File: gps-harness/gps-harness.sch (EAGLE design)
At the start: 7 parts

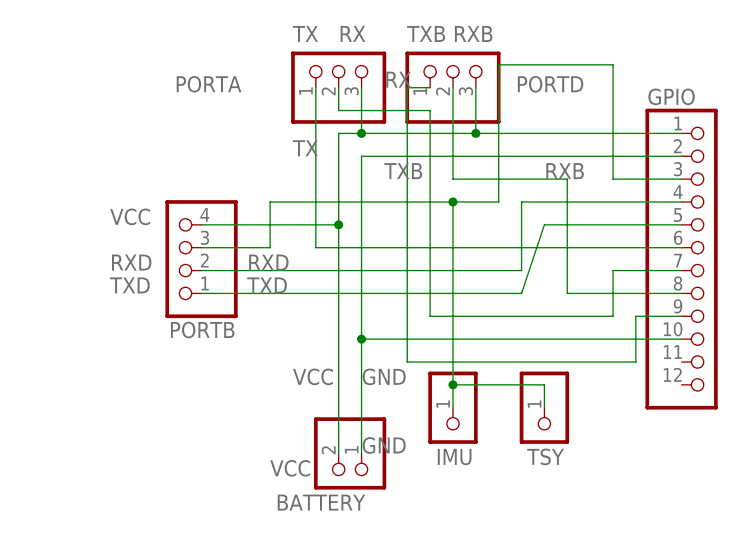
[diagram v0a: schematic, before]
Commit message: Fixed the width of the wires for battery and trying to do the mounting holes
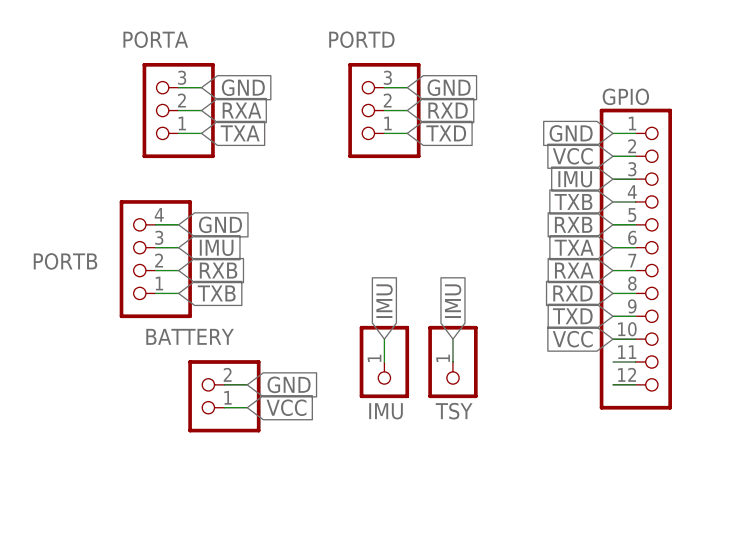
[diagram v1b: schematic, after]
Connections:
- net N$1 renamed IMU
- net RX renamed RXA
- net TX renamed TXA
- new net N$23: GPIO.11
- new net N$24: GPIO.12
- net GND: now also BATTERY.2, GPIO.1, PORTA.3, PORTB.4, PORTD.3; no longer BATTERY.1, GPIO.10, GPIO.2
- net RXB: now also GPIO.5, PORTB.2; no longer GPIO.8, PORTD.2
- net RXD: now also GPIO.8, PORTD.2; no longer GPIO.4, PORTB.2
- net TXB: now also GPIO.4, PORTB.1; no longer GPIO.9, PORTD.1
- net TXD: now also GPIO.9, PORTD.1; no longer GPIO.5, PORTB.1
- net VCC: now also BATTERY.1, GPIO.10, GPIO.2; no longer BATTERY.2, GPIO.1, PORTA.3, PORTB.4, PORTD.3
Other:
- moved on the sheet: BATTERY, GPIO, IMU, PORTA, PORTB, PORTD, TSY

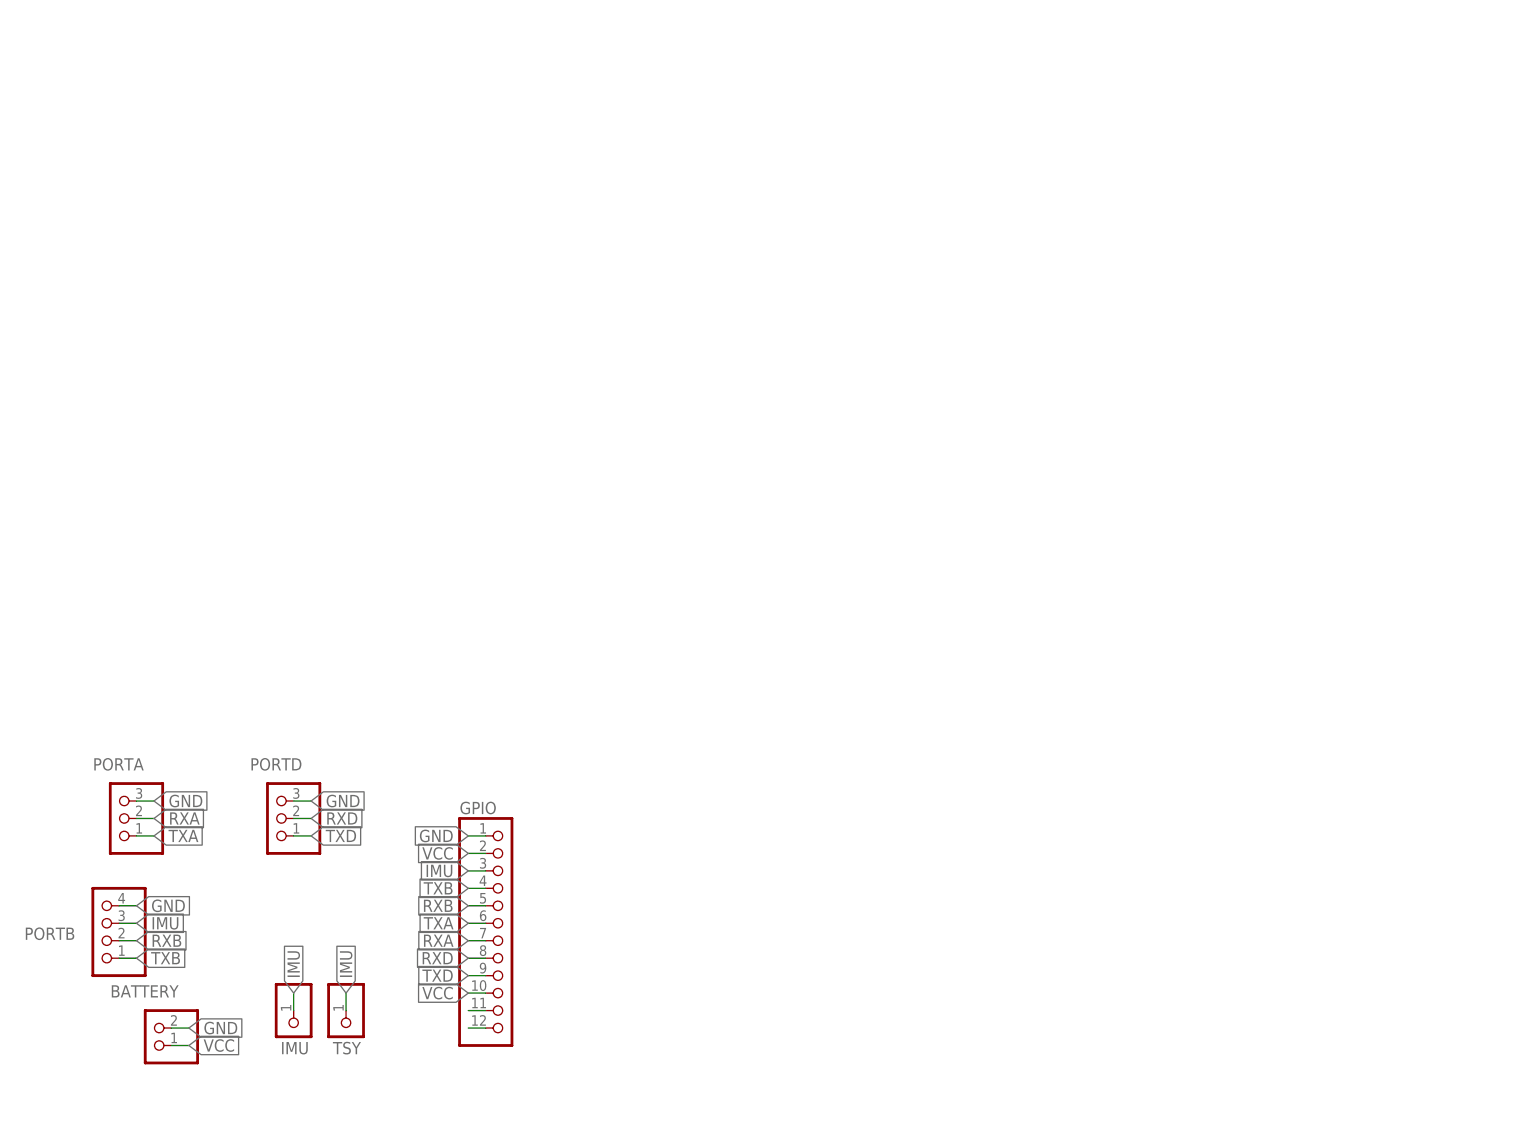
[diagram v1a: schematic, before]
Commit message: Change Schematic to Parts by parts
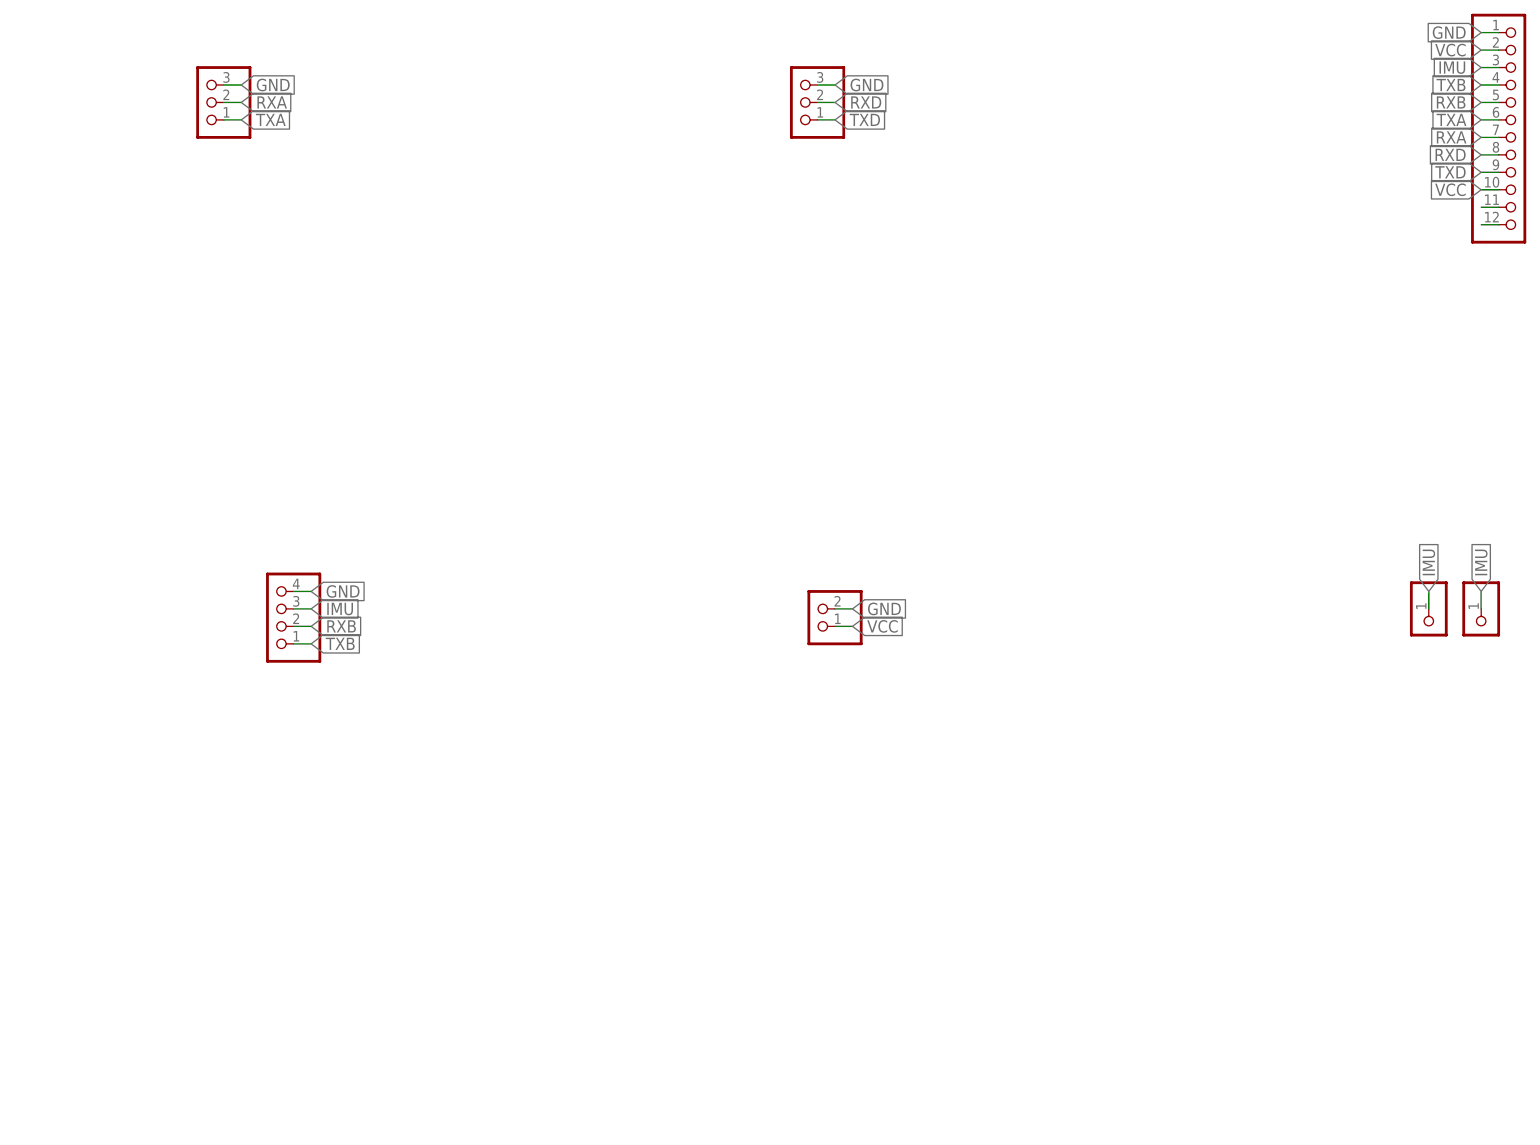
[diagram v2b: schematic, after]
